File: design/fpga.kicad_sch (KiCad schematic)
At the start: 83 parts, among them J7 DEBUG_FPGA_GPIO, J8 DIGILENT_JTAG_HS2_01X06, SW1 RST, SW2 PROG, U13 XC7S15-FTGB196, U14 IS25LP064A-JKx

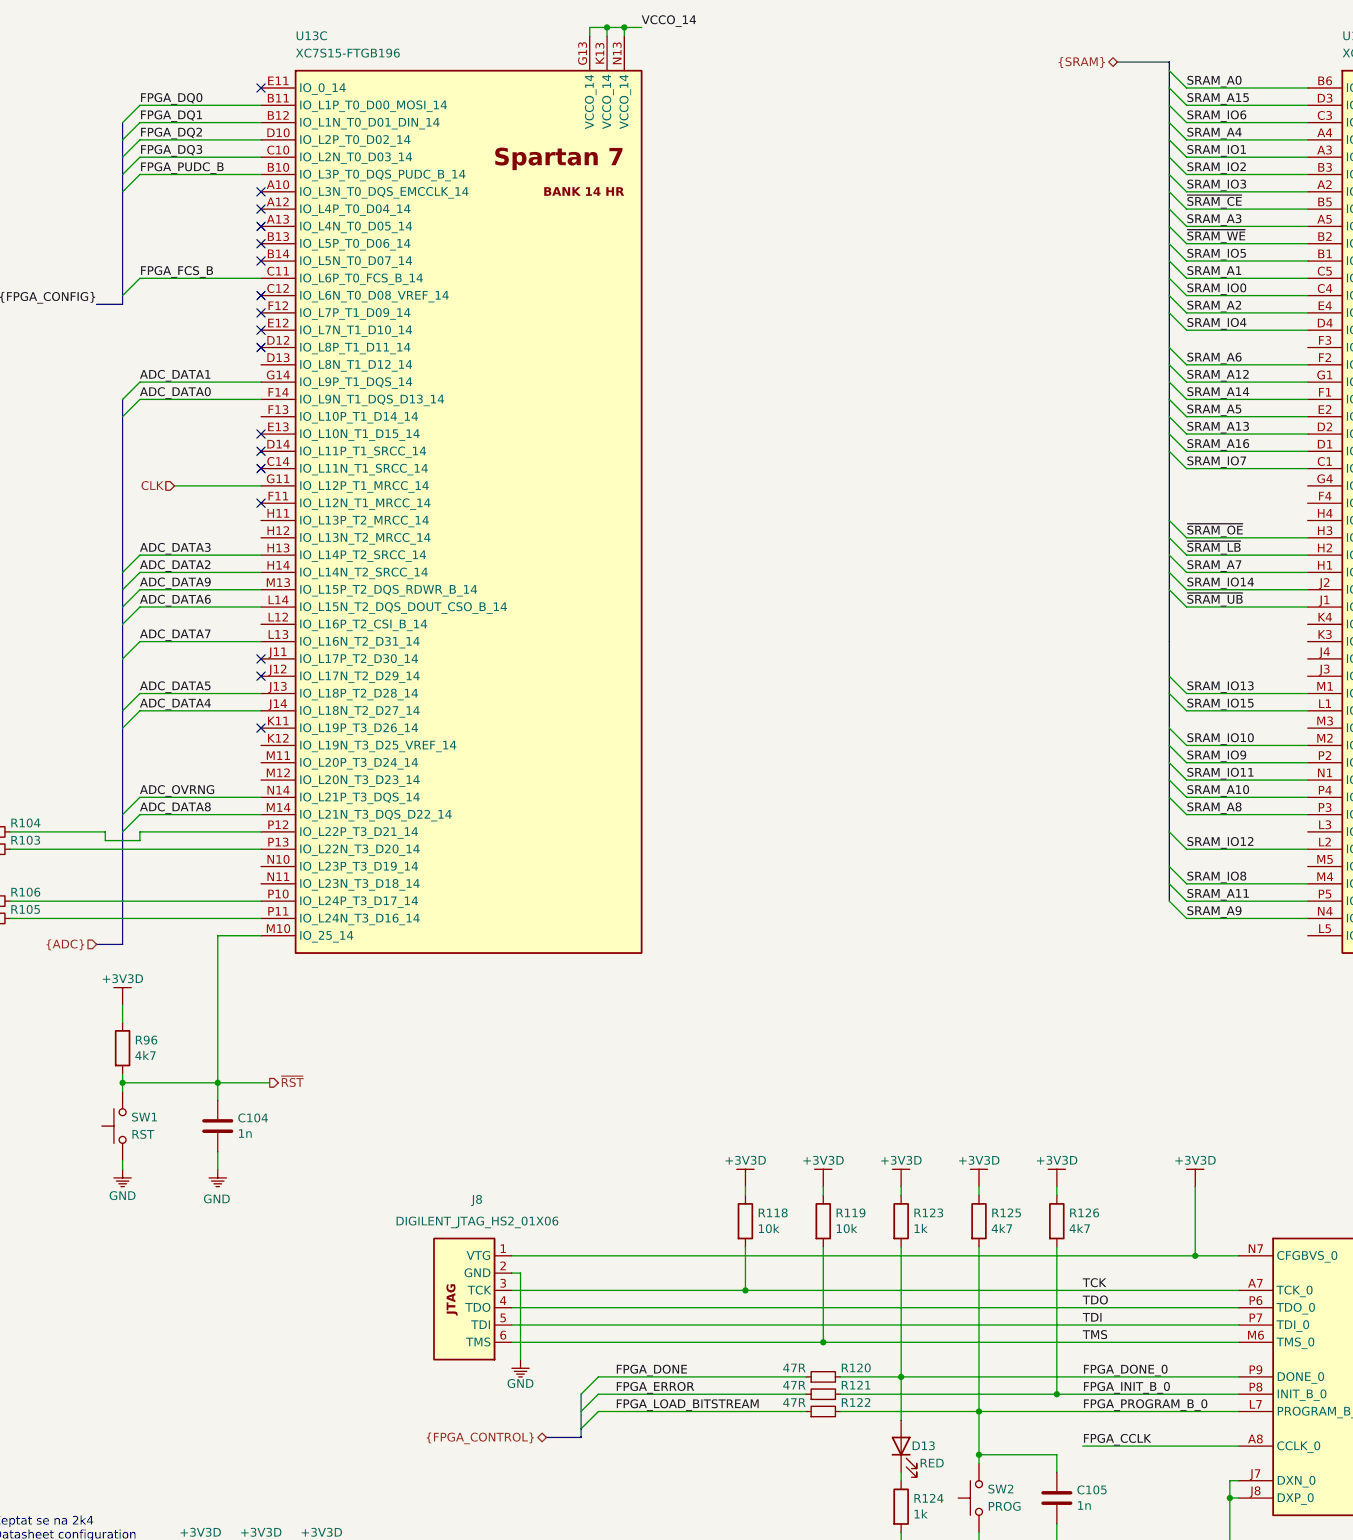
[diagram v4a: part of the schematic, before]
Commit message: Updated layout
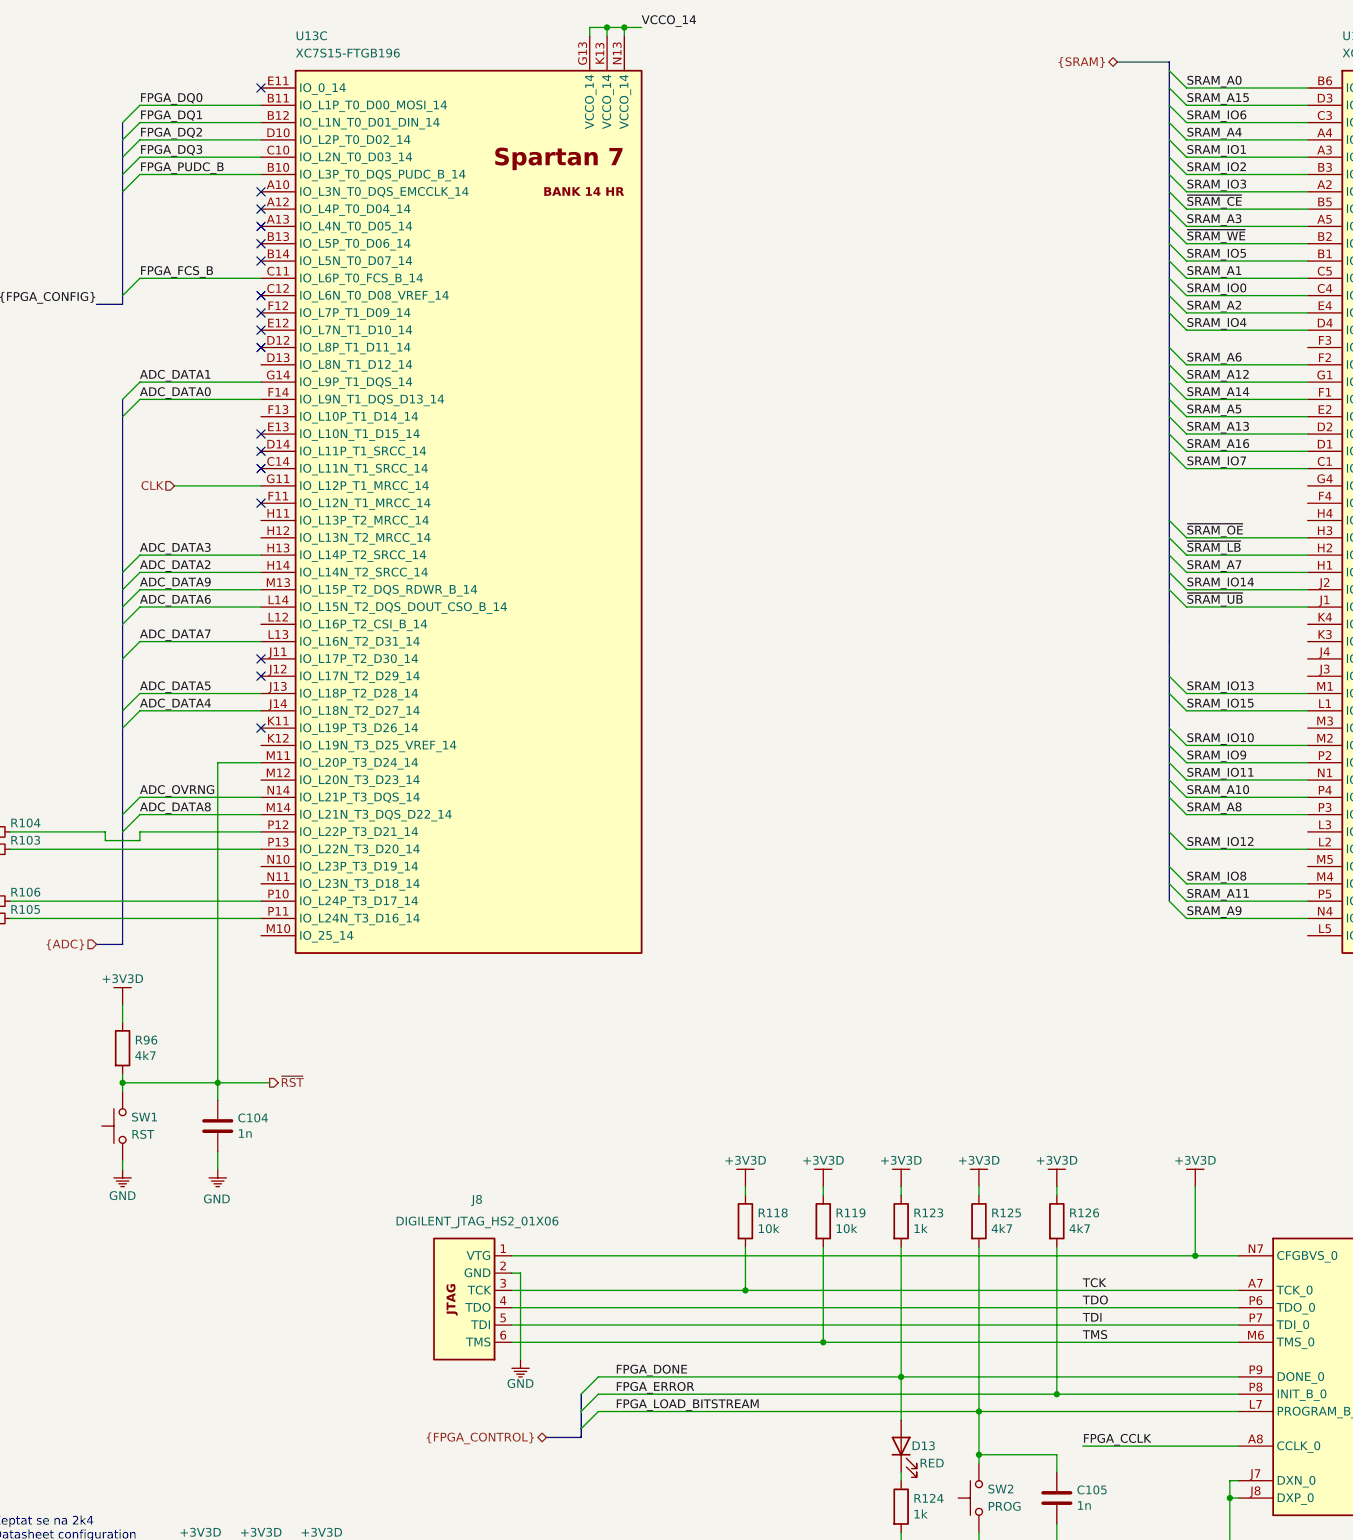
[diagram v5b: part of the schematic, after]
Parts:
- removed R120, R121, R122: 47R, Resistor_SMD:R_0402_1005Metric, symbol Device:R_Small
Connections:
- net FPGA_DONE_0 is gone; now on net FPGA_DONE: D13.2 (A), R123.2, U13.P9 (DONE_0)
- net FPGA_INIT_B_0 is gone; now on net FPGA_ERROR: R126.2, U13.P8 (INIT_B_0)
- net FPGA_PROGRAM_B_0 is gone; now on net FPGA_LOAD_BITSTREAM: C105.1, R125.2, SW2.2, U13.L7 (PROGRAM_B_0)
- net ~RST: now also U13.M11 (IO_L20P_T3_D24_14); no longer U13.M10 (IO_25_14)
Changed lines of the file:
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@@
 (kicad_sch (version 20200512) (host eeschema "5.99.0-unknown-2cf82d9~101~ubuntu18.04.1")
-  (page 1 8)
+  (page 8 8)
   (paper "A3")
   (title_block
@@
   (wire (pts (xy 176.53 250.19) (xy 176.53 267.97)))
   (wire (pts (xy 176.53 267.97) (xy 200.66 267.97)))
-  (wire (pts (xy 179.07 149.86) (xy 179.07 171.45)))
-  (wire (pts (xy 179.07 149.86) (xy 185.42 149.86)))
+  (wire (pts (xy 179.07 124.46) (xy 179.07 171.45)))
   (wire (pts (xy 179.07 171.45) (xy 179.07 173.99)))
   (wire (pts (xy 179.07 171.45) (xy 186.69 171.45)))
   (wire (pts (xy 179.07 181.61) (xy 179.07 184.15)))
+  (wire (pts (xy 185.42 124.46) (xy 179.07 124.46)))
   (wire (pts (xy 185.42 241.3) (xy 185.42 242.57)))
   (wire (pts (xy 185.42 250.19) (xy 185.42 260.35)))
@@
   (wire (pts (xy 233.68 16.51) (xy 236.22 16.51)))
   (wire (pts (xy 233.68 17.78) (xy 233.68 16.51)))
-  (wire (pts (xy 234.95 214.63) (xy 265.43 214.63)))
-  (wire (pts (xy 234.95 217.17) (xy 265.43 217.17)))
-  (wire (pts (xy 234.95 219.71) (xy 265.43 219.71)))
+  (wire (pts (xy 234.95 214.63) (xy 279.4 214.63)))
+  (wire (pts (xy 234.95 217.17) (xy 302.26 217.17)))
+  (wire (pts (xy 234.95 219.71) (xy 290.83 219.71)))
   (wire (pts (xy 236.22 16.51) (xy 236.22 17.78)))
   (wire (pts (xy 238.76 16.51) (xy 236.22 16.51)))
@@
   (wire (pts (xy 267.97 195.58) (xy 267.97 209.55)))
   (wire (pts (xy 267.97 209.55) (xy 328.93 209.55)))
-  (wire (pts (xy 270.51 214.63) (xy 279.4 214.63)))
-  (wire (pts (xy 270.51 217.17) (xy 302.26 217.17)))
-  (wire (pts (xy 270.51 219.71) (xy 290.83 219.71)))
   (wire (pts (xy 279.4 186.69) (xy 279.4 187.96)))
   (wire (pts (xy 279.4 195.58) (xy 279.4 214.63)))
@@
   (bus (pts (xy 161.29 151.13) (xy 165.1 151.13)))
   (bus (pts (xy 165.1 30.48) (xy 165.1 35.56)))
-  (bus (pts (xy 165.1 35.56) (xy 165.1 38.1)))
-  (bus (pts (xy 165.1 38.1) (xy 165.1 55.88)))
-  (bus (pts (xy 165.1 55.88) (xy 165.1 57.15)))
+  (bus (pts (xy 165.1 35.56) (xy 165.1 40.64)))
+  (bus (pts (xy 165.1 40.64) (xy 165.1 57.15)))
   (bus (pts (xy 165.1 71.12) (xy 165.1 96.52)))
   (bus (pts (xy 165.1 96.52) (xy 165.1 101.6)))
@@
   (bus (pts (xy 318.77 21.59) (xy 318.77 25.4)))
   (bus (pts (xy 318.77 25.4) (xy 318.77 30.48)))
-  (bus (pts (xy 318.77 30.48) (xy 318.77 33.02)))
-  (bus (pts (xy 318.77 33.02) (xy 318.77 38.1)))
-  (bus (pts (xy 318.77 38.1) (xy 318.77 43.18)))
+  (bus (pts (xy 318.77 30.48) (xy 318.77 35.56)))
+  (bus (pts (xy 318.77 35.56) (xy 318.77 40.64)))
+  (bus (pts (xy 318.77 40.64) (xy 318.77 43.18)))
   (bus (pts (xy 318.77 43.18) (xy 318.77 48.26)))
   (bus (pts (xy 318.77 48.26) (xy 318.77 53.34)))
@@
   (bus (pts (xy 318.77 71.12) (xy 318.77 76.2)))
   (bus (pts (xy 318.77 76.2) (xy 318.77 88.9)))
-  (bus (pts (xy 318.77 88.9) (xy 318.77 91.44)))
-  (bus (pts (xy 318.77 91.44) (xy 318.77 96.52)))
-  (bus (pts (xy 318.77 96.52) (xy 318.77 106.68)))
+  (bus (pts (xy 318.77 88.9) (xy 318.77 93.98)))
+  (bus (pts (xy 318.77 93.98) (xy 318.77 99.06)))
+  (bus (pts (xy 318.77 99.06) (xy 318.77 106.68)))
   (bus (pts (xy 318.77 106.68) (xy 318.77 114.3)))
   (bus (pts (xy 318.77 114.3) (xy 318.77 121.92)))
@@
     (effects (font (size 1.27 1.27)) (justify left bottom))
   )
-  (label "FPGA_DONE_0" (at 306.07 214.63 0)
-    (effects (font (size 1.27 1.27)) (justify left bottom))
-  )
-  (label "FPGA_INIT_B_0" (at 306.07 217.17 0)
-    (effects (font (size 1.27 1.27)) (justify left bottom))
-  )
-  (label "FPGA_PROGRAM_B_0" (at 306.07 219.71 0)
-    (effects (font (size 1.27 1.27)) (justify left bottom))
-  )
   (label "FPGA_CCLK" (at 306.07 224.79 0)
     (effects (font (size 1.27 1.27)) (justify left bottom))
@@
       (effects (font (size 1.27 1.27)) hide)
     )
-  )
-  (symbol (lib_id "Device:R_Small") (at 267.97 214.63 90) (unit 1)
-    (property "Reference" "R120" (id 0) (at 270.51 213.36 90)
-      (effects (font (size 1.27 1.27)) (justify right))
-    )
-    (property "Value" "47R" (id 1) (at 265.43 213.36 90)
-      (effects (font (size 1.27 1.27)) (justify left))
-    )
-    (property "Footprint" "Resistor_SMD:R_0402_1005Metric" (id 2) (at 267.97 214.63 0)
-      (effects (font (size 1.27 1.27)) hide)
-    )
-    (property "Datasheet" "~" (id 3) (at 267.97 214.63 0)
-      (effects (font (size 1.27 1.27)) hide)
-    )
-  )
-  (symbol (lib_id "Device:R_Small") (at 267.97 217.17 90) (unit 1)
-    (property "Reference" "R121" (id 0) (at 270.51 215.9 90)
-      (effects (font (size 1.27 1.27)) (justify right))
-    )
-    (property "Value" "47R" (id 1) (at 265.43 215.9 90)
-      (effects (font (size 1.27 1.27)) (justify left))
-    )
-    (property "Footprint" "Resistor_SMD:R_0402_1005Metric" (id 2) (at 267.97 217.17 0)
-      (effects (font (size 1.27 1.27)) hide)
-    )
-    (property "Datasheet" "~" (id 3) (at 267.97 217.17 0)
-      (effects (font (size 1.27 1.27)) hide)
-    )
-  )
-  (symbol (lib_id "Device:R_Small") (at 267.97 219.71 90) (unit 1)
-    (property "Reference" "R122" (id 0) (at 270.51 218.44 90)
-      (effects (font (size 1.27 1.27)) (justify right))
-    )
-    (property "Value" "47R" (id 1) (at 265.43 218.44 90)
-      (effects (font (size 1.27 1.27)) (justify left))
-    )
-    (property "Footprint" "Resistor_SMD:R_0402_1005Metric" (id 2) (at 267.97 219.71 0)
-      (effects (font (size 1.27 1.27)) hide)
-    )
-    (property "Datasheet" "~" (id 3) (at 267.97 219.71 0)
-      (effects (font (size 1.27 1.27)) hide)
-    )
